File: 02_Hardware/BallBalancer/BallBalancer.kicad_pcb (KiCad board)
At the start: 2 copper layers, 64.5 x 77 mm, 128 parts, among them J1 USB_B_Micro, J2 Raspberry PI UART, J3 SWD, J4 Reference switch 1, J5 ENCODER 1, J6 ENCODER 2, J7 Reference switch 2, J8 Jack-DC, M1 Motor_DC, M2 Motor_DC, Q1 DMN10H220L, Q2 DMN10H220L, Q3 DMN10H220L, Q4 DMN10H220L, Q5 DMN10H220L, Q6 DMN10H220L, Q7 DMN10H220L, Q8 DMN10H220L, U1 STM32L412K8Tx, U2 USBLC6-2SC6, U3 DGD0506A, U4 DGD0506A, U5 LM2937IMP5, U6 AP63203WU, U7 DGD0506A, U8 DGD0506A

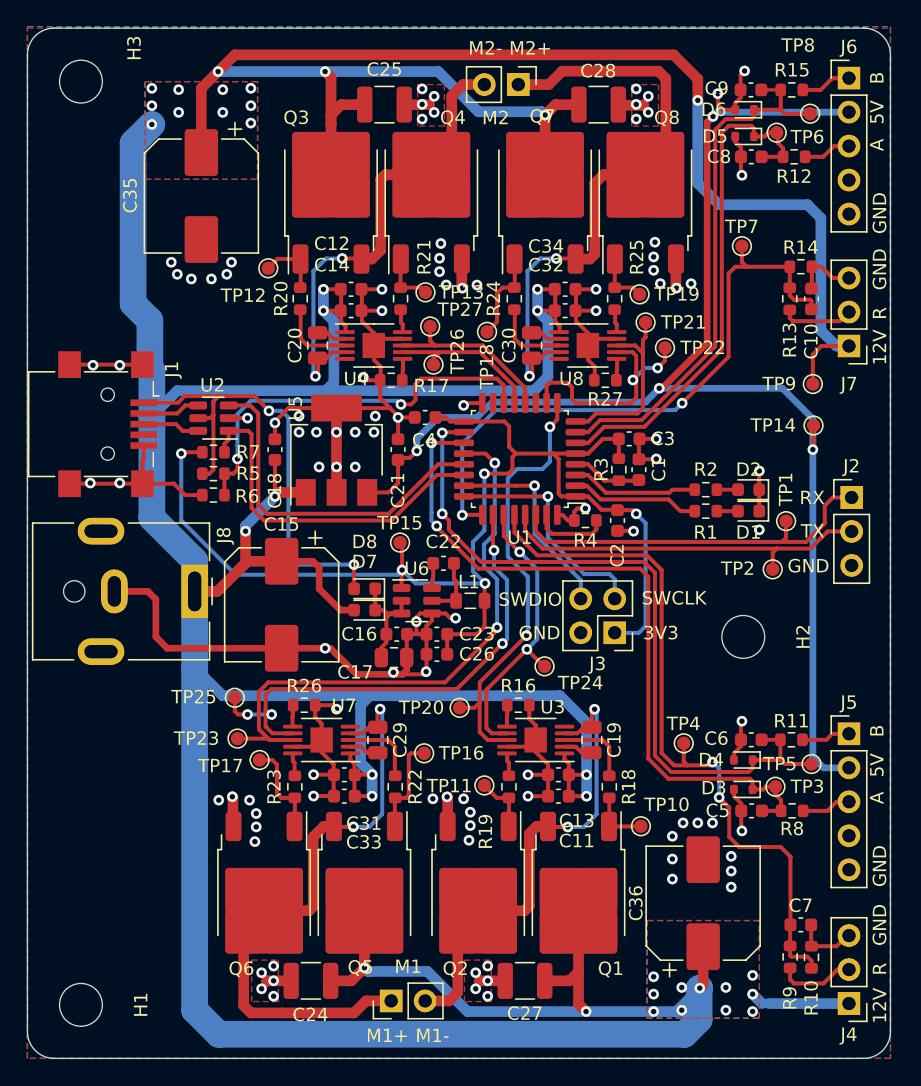
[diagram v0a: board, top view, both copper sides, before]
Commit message: replace microcontroller
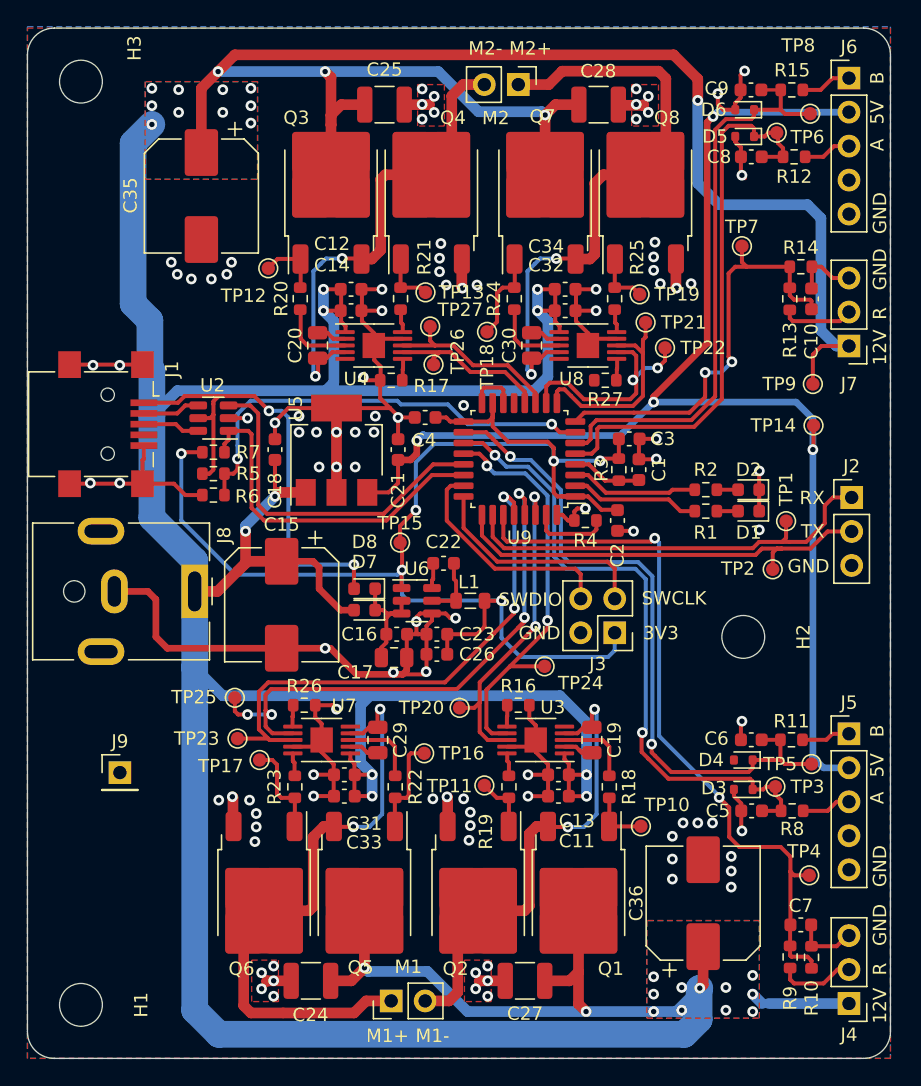
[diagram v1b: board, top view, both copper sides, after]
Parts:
- removed U1: STM32L412K8Tx, Package_QFP:LQFP-32_7x7mm_P0.8mm
- added J9: GND, Connector_PinHeader_2.54mm:PinHeader_1x01_P2.54mm_Vertical, F.Cu at (89.4, 113.6)
- added U9: STM32G431K8Tx, Package_QFP:LQFP-32_7x7mm_P0.8mm, F.Cu at (119.3, 90.2)
- moved TP4 13.6 mm to (140.9, 121.3)
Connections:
- J2 pad 1: /Main/RSPI_RX -> /Main/RSPI_TX
- J2 pad 2: /Main/RSPI_TX -> /Main/RSPI_RX
- TP1 pad 1: /Main/RSPI_RX -> /Main/RSPI_TX
- TP2 pad 1: /Main/RSPI_TX -> /Main/RSPI_RX
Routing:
- net /Main/REF_MOT2: track 46.7 -> 32.3 mm
- net +3V3: track 93.7 -> 106.1 mm, vias 5 -> 6
- net EN_MOT_CH1L: track 22.1 -> 31.4 mm
- net IN_MOT_CH1L: track 33.3 -> 24.7 mm
- net /Main/ENCODER1_A: track 54.1 -> 48.7 mm
- net /Main/ENCODER1_B: track 55.5 -> 50.9 mm
- net /Main/RSPI_TX: track 28.4 -> 32.8 mm
- net EN_MOT_CH1R: track 38.5 -> 42.9 mm
- net /Main/RSPI_RX: track 29.0 -> 32.6 mm
- net /Main/ENCODER2_A: track 38.8 -> 42.2 mm
- net /Main/VUSB: track 30.3 -> 33.5 mm
- net IN_MOT_CH1R: track 43.7 -> 40.5 mm
- net /Main/ENCODER2_B: track 40.0 -> 43.1 mm
- net /Main/SWDIO: track 15.2 -> 17.2 mm, vias 1 -> 0
- net GND: track 193.2 -> 191.2 mm
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
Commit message: Layout completed with stm32g431
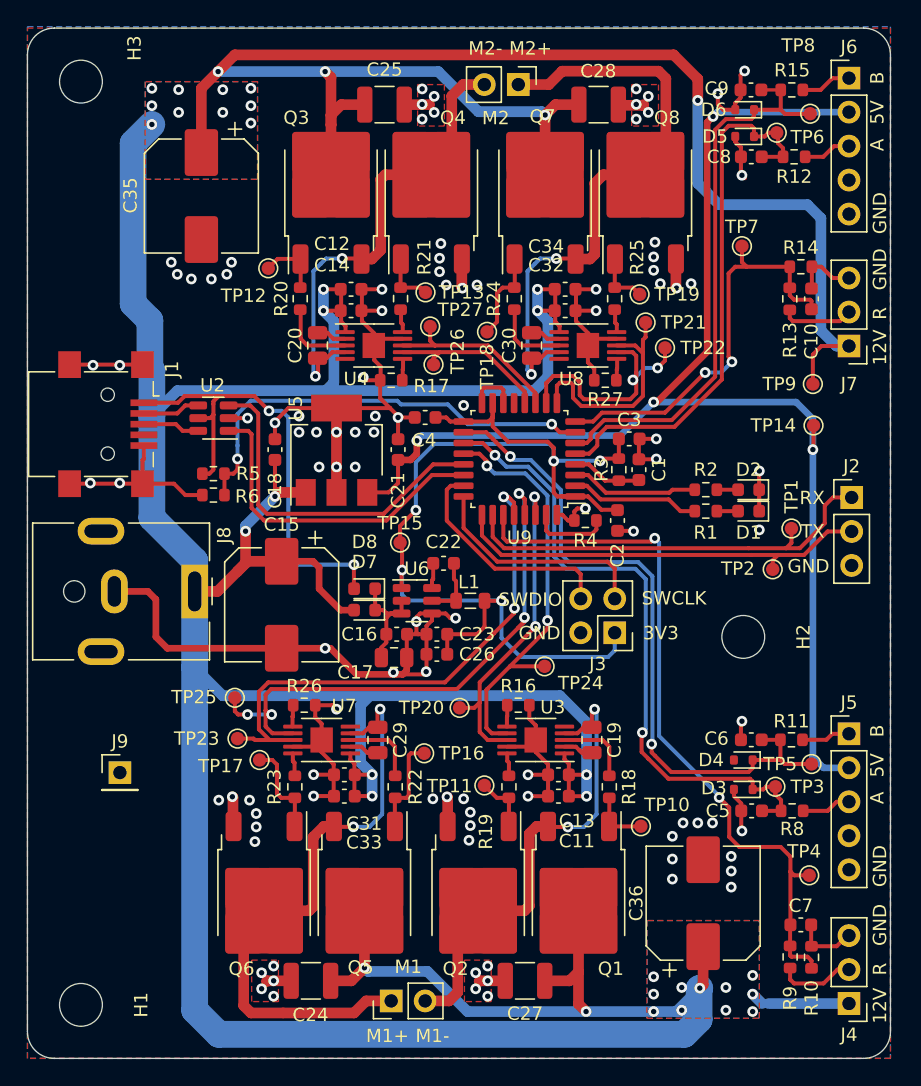
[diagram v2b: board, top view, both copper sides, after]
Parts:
- removed R7: 1.5k, Resistor_SMD:R_0603_1608Metric
- R18, R19, R20, R21, R22, R23, R24, R25: value 120 -> 22
- moved TP1 0.68 mm to (139.6, 95.4)
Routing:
- net +3V3: track 106.1 -> 81.2 mm, vias 6 -> 5
- net GND: track 191.2 -> 194.0 mm
- net /Main/USB_DP: track 26.7 -> 25.0 mm
- net /Main/ENCODER2_A: track 42.2 -> 40.9 mm
- net IN_MOT_CH2R: track 16.0 -> 17.2 mm
- net /Main/ENCODER2_B: track 43.1 -> 41.9 mm
- net EN_MOT_CH2R: track 17.8 -> 18.9 mm
- net /Main/REF_MOT2: track 32.3 -> 31.3 mm
- net /Main/RSPI_RX: track 32.6 -> 31.7 mm

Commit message: update layout
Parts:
- removed J9: GND, Connector_PinHeader_2.54mm:PinHeader_1x01_P2.54mm_Vertical
- added J10: GND, Connector_PinHeader_2.54mm:PinHeader_1x02_P2.54mm_Vertical, F.Cu at (89.4, 113.7)
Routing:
- net +12V: track 429.7 -> 450.3 mm, vias 37 -> 46
- net GND: track 194.0 -> 193.6 mm, vias 103 -> 102
